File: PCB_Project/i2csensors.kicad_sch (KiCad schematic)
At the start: 20 parts

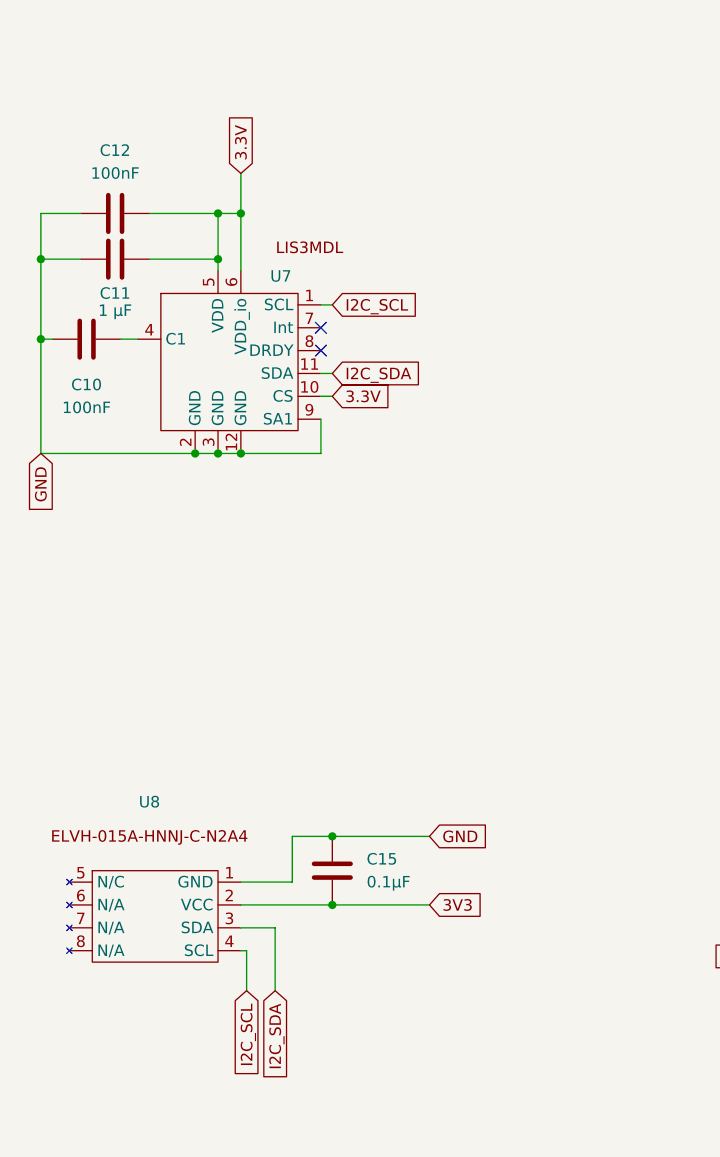
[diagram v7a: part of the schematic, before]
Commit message: I2C pullups added
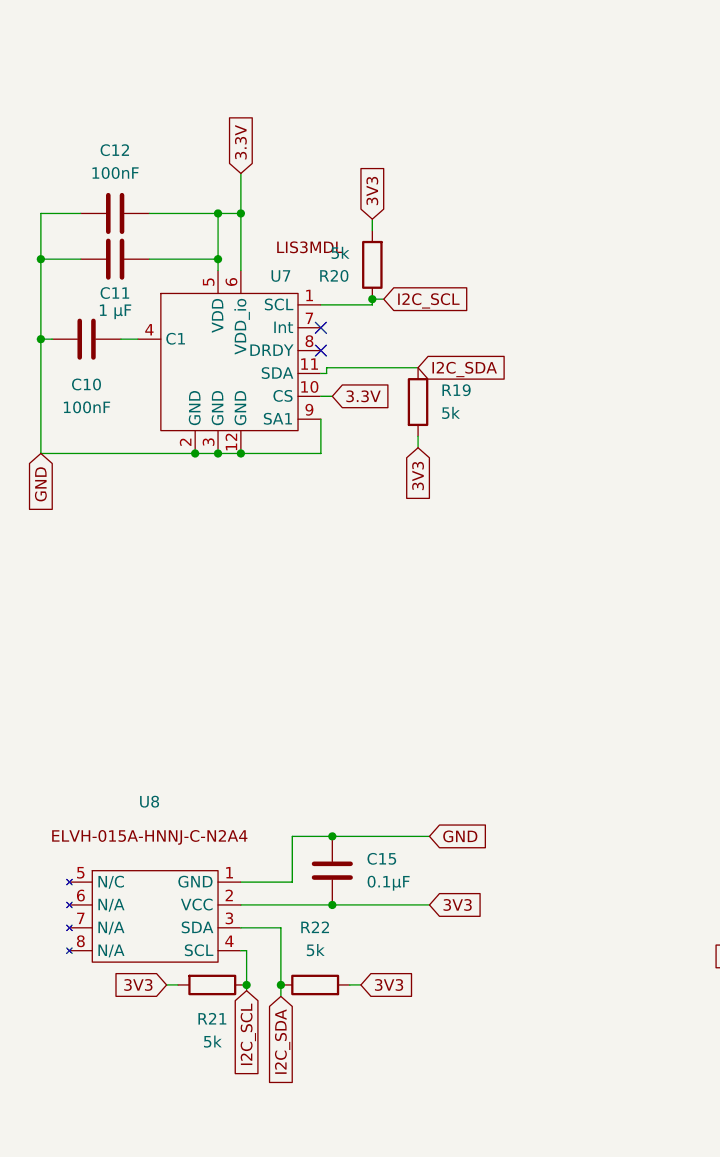
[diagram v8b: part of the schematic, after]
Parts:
- added R19, R20, R21, R22: 5k, symbol Device:R
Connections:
- net 3V3: now also R19.2, R20.2, R21.2, R22.2
- net I2C_SCL: now also R20.1, R21.1
- net I2C_SDA: now also R19.1, R22.1
